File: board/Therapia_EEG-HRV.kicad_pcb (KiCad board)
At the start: 4 copper layers, 61.8 x 45 mm, 141 parts, among them J1 USB-C_16P, J2 Header_2x6

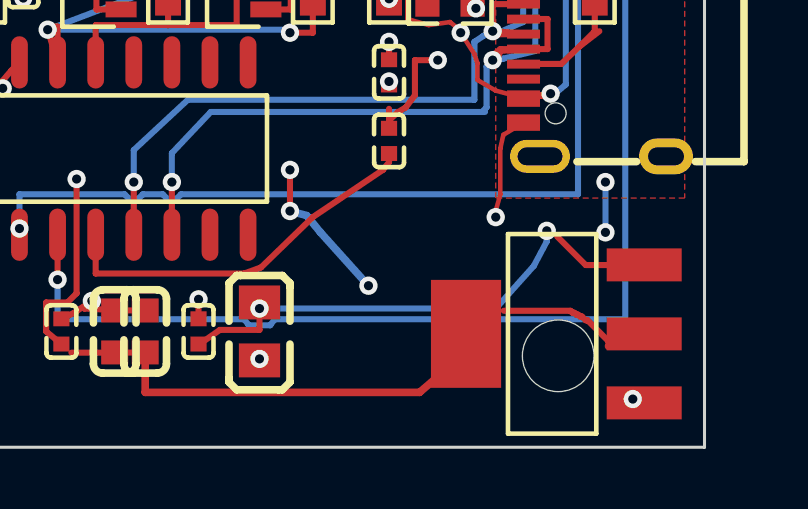
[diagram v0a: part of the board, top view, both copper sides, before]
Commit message: S5 L3: split the ESP_TXD track and route its middle clear of H4
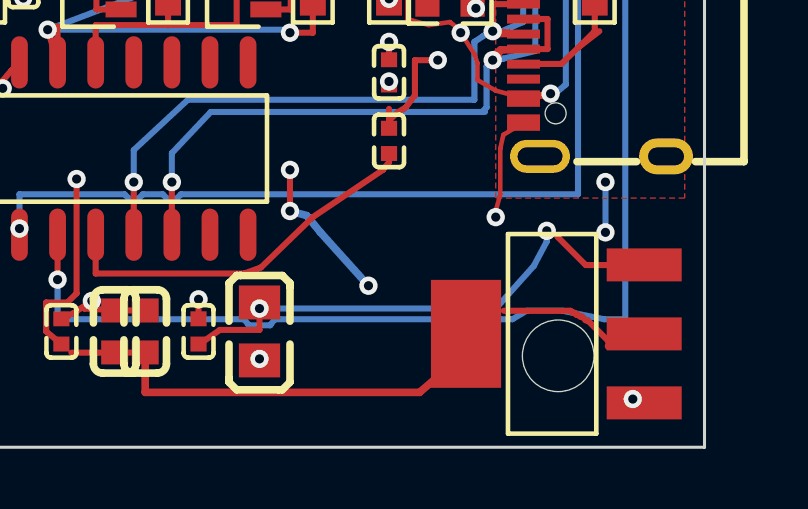
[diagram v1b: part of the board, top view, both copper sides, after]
